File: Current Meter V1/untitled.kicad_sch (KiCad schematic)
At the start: 10 parts, among them J401 I2C OLED Display Connector

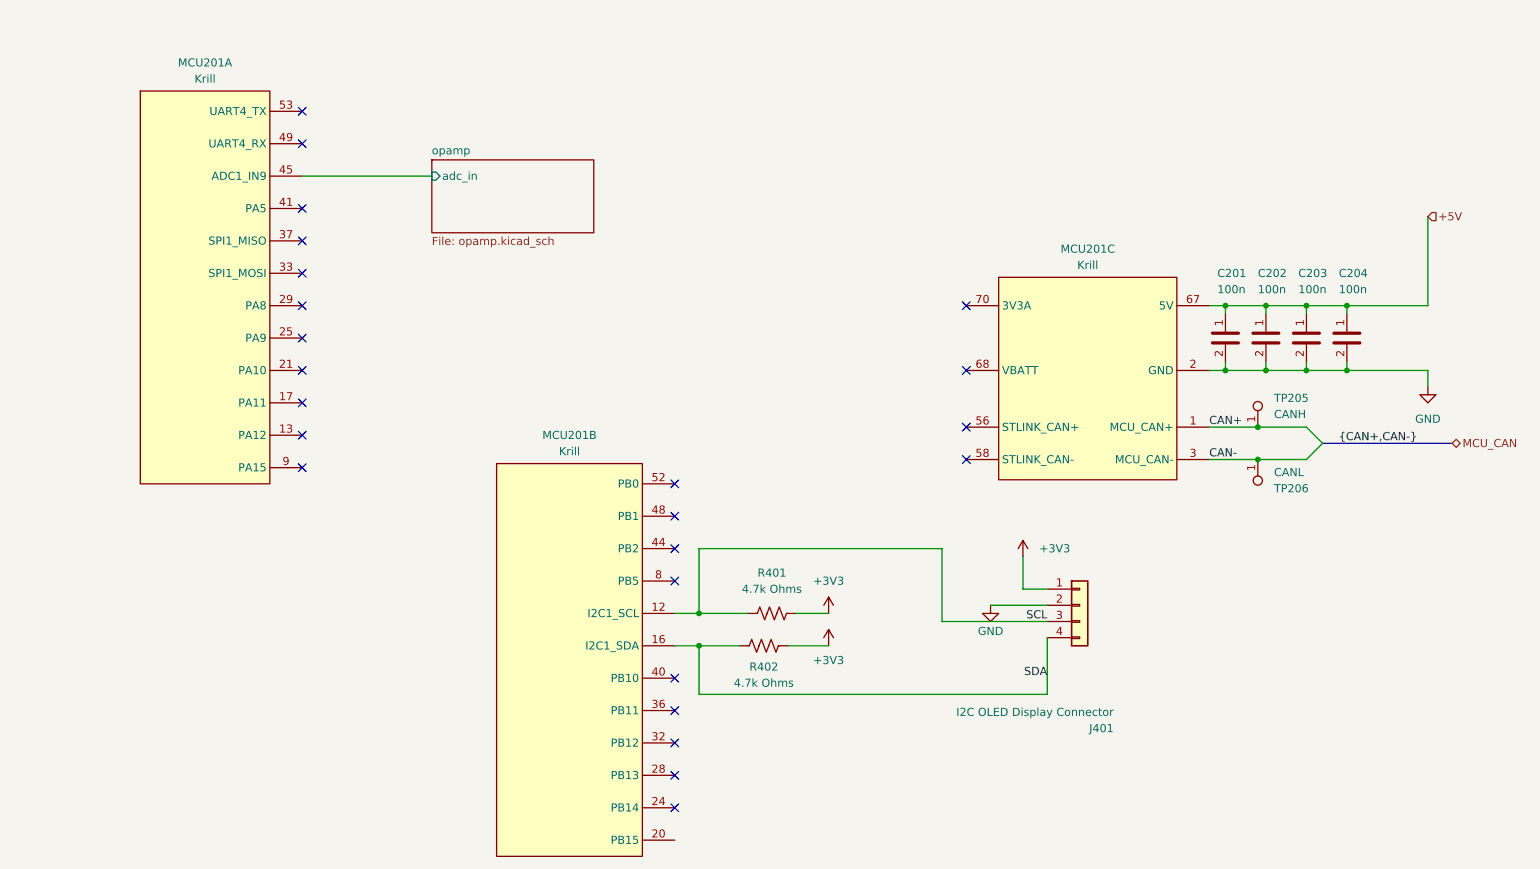
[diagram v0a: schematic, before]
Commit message: can differential pair
added can bus to microcontroller, and started labeling the pins on the microcontroller
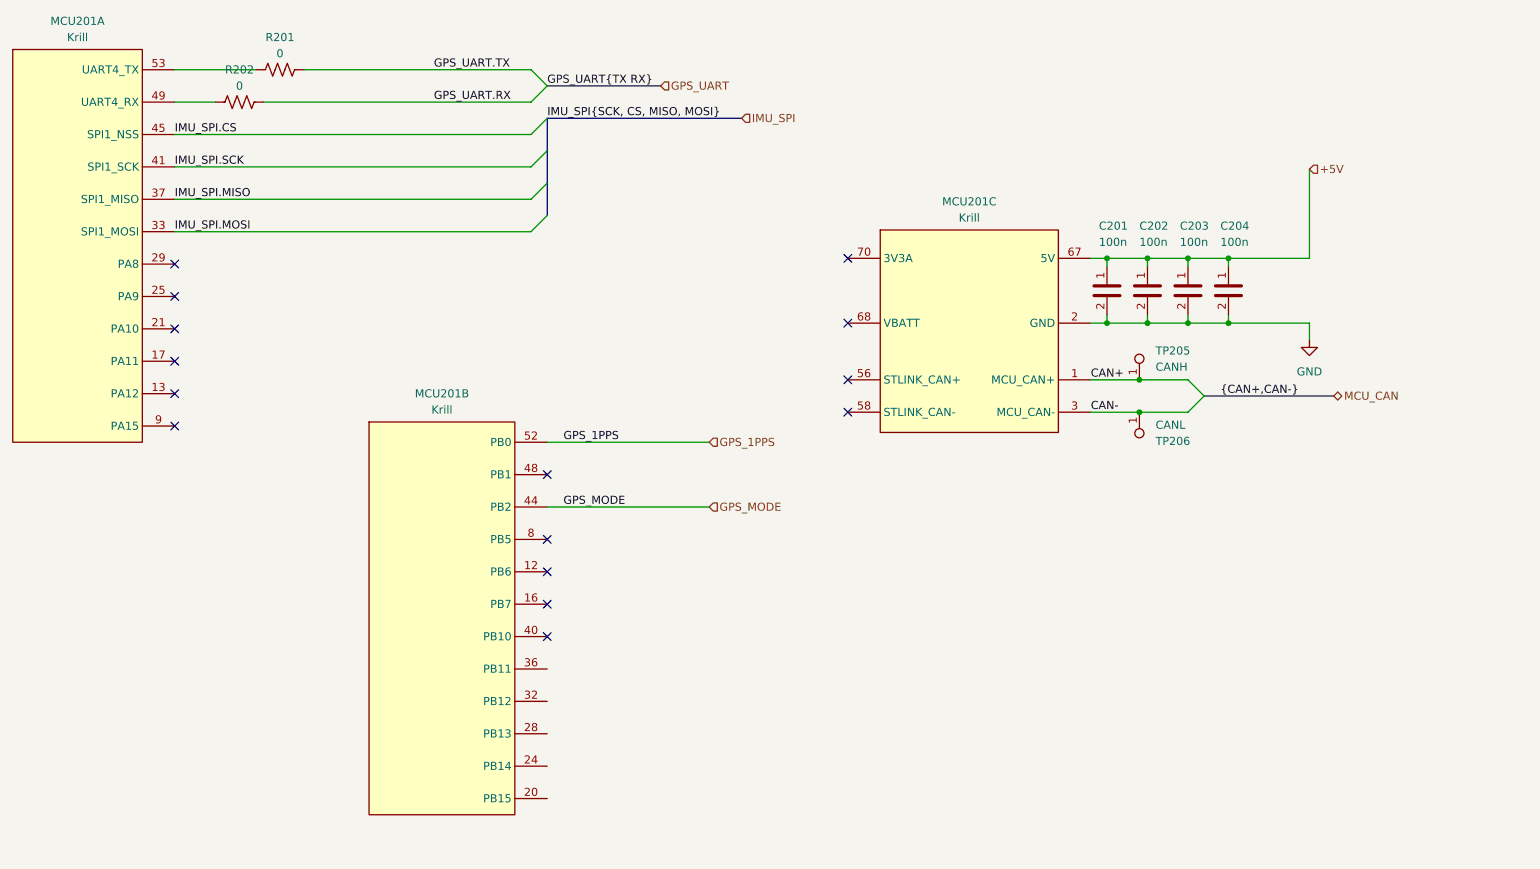
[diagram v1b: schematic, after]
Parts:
- removed J401: I2C OLED Display Connector, symbol Connector_Generic:Conn_01x04
- removed R401, R402: 4.7k Ohms, symbol Device:R_US
- added R201, R202: 0, Resistor_SMD:R_0603_1608Metric_Pad0.98x0.95mm_HandSolder, symbol bfr_resistors:RMCF0603ZT0R00
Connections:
- net IMU_SPI.MOSI: now reaches MCU201.33 (PA7)
- net IMU_SPI.MISO: now reaches MCU201.37 (PA6)
- net IMU_SPI.SCK: now reaches MCU201.41 (PA5)
- net at MCU201.49 (PA1): now also R202.1
- net at MCU201.53 (PA0): now also R201.1
- net GPS_MODE: now reaches MCU201.44 (PB2)
- net GPS_1PPS: now reaches MCU201.52 (PB0)
- net SCL: no longer names the net of MCU201.12 (PB6)
- net SDA: no longer names the net of MCU201.16 (PB7)
- net opamp/adc_in renamed IMU_SPI.CS
- new net GPS_UART.RX: R202.2
- new net GPS_UART.TX: R201.2
- no-connect marks 24 -> 15
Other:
- removed sheet opamp
- moved on the sheet: C201, C202, C203, C204, MCU201A, MCU201B, MCU201C, TP205, TP206
